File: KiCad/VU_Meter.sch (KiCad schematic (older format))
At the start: 34 parts

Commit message: changed Q to a fixed value
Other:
- moved on the sheet: D?, R?, U?

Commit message: saved from laptop and added new questions
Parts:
- U? (x15): symbol Comparator:LM393 -> Amp-Module-rescue:LM393-Comparator
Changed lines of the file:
@@
 $EndDescr
 $Comp
-L Comparator:LM393 U?
+L Amp-Module-rescue:LM393-Comparator U?
 U 3 1 60442CB7
 P 8200 4050
+AR Path="/60442CB7" Ref="U?"  Part="3"
+AR Path="/603D6377/60442CB7" Ref="U?"  Part="3"
 F 0 "U?" V 7900 4050 50  0000 C CNN
 F 1 "LM393" V 8000 4050 50  0000 C CNN
@@
 +5VDC
 $Comp
-L Comparator:LM393 U?
+L Amp-Module-rescue:LM393-Comparator U?
 U 1 1 60442CBE
 P 10400 3750
+AR Path="/60442CBE" Ref="U?"  Part="1"
+AR Path="/603D6377/60442CBE" Ref="U?"  Part="1"
 F 0 "U?" H 10400 3950 50  0000 C CNN
 F 1 "LM393" H 10400 3750 50  0000 C CNN
@@
 $EndComp
 $Comp
-L Comparator:LM393 U?
+L Amp-Module-rescue:LM393-Comparator U?
 U 2 1 60442CC4
 P 10400 4250
+AR Path="/60442CC4" Ref="U?"  Part="2"
+AR Path="/603D6377/60442CC4" Ref="U?"  Part="2"
 F 0 "U?" H 10400 4450 50  0000 C CNN
 F 1 "LM393" H 10400 4250 50  0000 C CNN
@@
 $EndComp
 $Comp
-L Comparator:LM393 U?
+L Amp-Module-rescue:LM393-Comparator U?
 U 2 1 60442CCA
 P 10400 5250
+AR Path="/60442CCA" Ref="U?"  Part="2"
+AR Path="/603D6377/60442CCA" Ref="U?"  Part="2"
 F 0 "U?" H 10400 5450 50  0000 C CNN
 F 1 "LM393" H 10400 5250 50  0000 C CNN
@@
 VOUT MONITOR
 $Comp
-L Comparator:LM393 U?
+L Amp-Module-rescue:LM393-Comparator U?
 U 3 1 60442D23
 P 8200 4400
+AR Path="/60442D23" Ref="U?"  Part="3"
+AR Path="/603D6377/60442D23" Ref="U?"  Part="3"
 F 0 "U?" V 7900 4400 50  0000 C CNN
 F 1 "LM393" V 8000 4400 50  0000 C CNN
@@
 $EndComp
 $Comp
-L Comparator:LM393 U?
+L Amp-Module-rescue:LM393-Comparator U?
 U 3 1 60442D29
 P 8200 4750
+AR Path="/60442D29" Ref="U?"  Part="3"
+AR Path="/603D6377/60442D29" Ref="U?"  Part="3"
 F 0 "U?" V 7900 4750 50  0000 C CNN
 F 1 "LM393" V 8000 4750 50  0000 C CNN
@@
 $EndComp
 $Comp
-L Comparator:LM393 U?
+L Amp-Module-rescue:LM393-Comparator U?
 U 3 1 60442D2F
 P 8200 5100
+AR Path="/60442D2F" Ref="U?"  Part="3"
+AR Path="/603D6377/60442D2F" Ref="U?"  Part="3"
 F 0 "U?" V 7900 5100 50  0000 C CNN
 F 1 "LM393" V 8000 5100 50  0000 C CNN
@@
 $EndComp
 $Comp
-L Comparator:LM393 U?
+L Amp-Module-rescue:LM393-Comparator U?
 U 3 1 60442D35
 P 8200 5450
+AR Path="/60442D35" Ref="U?"  Part="3"
+AR Path="/603D6377/60442D35" Ref="U?"  Part="3"
 F 0 "U?" V 7900 5450 50  0000 C CNN
 F 1 "LM393" V 8000 5450 50  0000 C CNN
@@
 $EndComp
 $Comp
-L Comparator:LM393 U?
+L Amp-Module-rescue:LM393-Comparator U?
 U 1 1 60442D72
 P 10400 4750
+AR Path="/60442D72" Ref="U?"  Part="1"
+AR Path="/603D6377/60442D72" Ref="U?"  Part="1"
 F 0 "U?" H 10400 4950 50  0000 C CNN
 F 1 "LM393" H 10400 4750 50  0000 C CNN
@@
 	9950 5150 9950 5200
 $Comp
-L Comparator:LM393 U?
+L Amp-Module-rescue:LM393-Comparator U?
 U 1 1 60442D88
 P 10400 1200
+AR Path="/60442D88" Ref="U?"  Part="1"
+AR Path="/603D6377/60442D88" Ref="U?"  Part="1"
 F 0 "U?" H 10400 1400 50  0000 C CNN
 F 1 "LM393" H 10400 1200 50  0000 C CNN
@@
 $EndComp
 $Comp
-L Comparator:LM393 U?
+L Amp-Module-rescue:LM393-Comparator U?
 U 2 1 60442D8E
 P 10400 1700
+AR Path="/60442D8E" Ref="U?"  Part="2"
+AR Path="/603D6377/60442D8E" Ref="U?"  Part="2"
 F 0 "U?" H 10400 1900 50  0000 C CNN
 F 1 "LM393" H 10400 1700 50  0000 C CNN
@@
 $EndComp
 $Comp
-L Comparator:LM393 U?
+L Amp-Module-rescue:LM393-Comparator U?
 U 2 1 60442D94
 P 10400 2700
+AR Path="/60442D94" Ref="U?"  Part="2"
+AR Path="/603D6377/60442D94" Ref="U?"  Part="2"
 F 0 "U?" H 10400 2900 50  0000 C CNN
 F 1 "LM393" H 10400 2700 50  0000 C CNN
@@
 	11050 1200 11050 1700
 $Comp
-L Comparator:LM393 U?
+L Amp-Module-rescue:LM393-Comparator U?
 U 1 1 60442DEA
 P 10400 2200
+AR Path="/60442DEA" Ref="U?"  Part="1"
+AR Path="/603D6377/60442DEA" Ref="U?"  Part="1"
 F 0 "U?" H 10400 2400 50  0000 C CNN
 F 1 "LM393" H 10400 2200 50  0000 C CNN
@@
 LM_VOUT3MON
 $Comp
-L Comparator:LM393 U?
+L Amp-Module-rescue:LM393-Comparator U?
 U 1 1 60442E29
 P 8650 2750
+AR Path="/60442E29" Ref="U?"  Part="1"
+AR Path="/603D6377/60442E29" Ref="U?"  Part="1"
 F 0 "U?" H 8650 2950 50  0000 C CNN
 F 1 "LM393" H 8650 2750 50  0000 C CNN
@@
 $EndComp
 $Comp
-L Comparator:LM393 U?
+L Amp-Module-rescue:LM393-Comparator U?
 U 2 1 60442E2F
 P 8650 3400
+AR Path="/60442E2F" Ref="U?"  Part="2"
+AR Path="/603D6377/60442E2F" Ref="U?"  Part="2"
 F 0 "U?" H 8650 3600 50  0000 C CNN
 F 1 "LM393" H 8650 3400 50  0000 C CNN

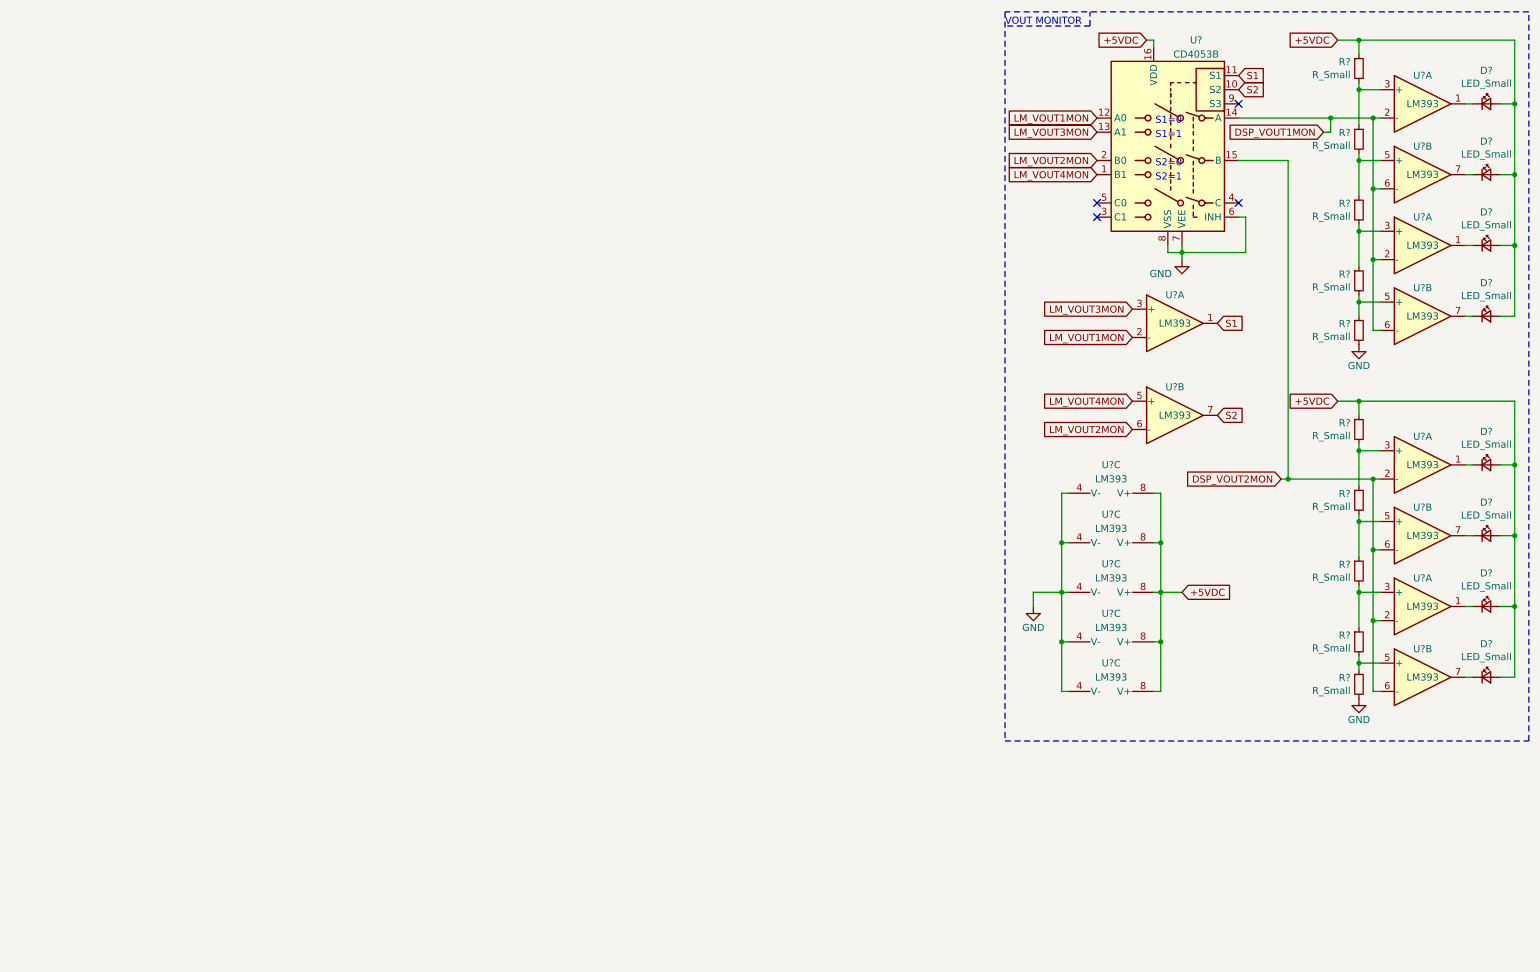
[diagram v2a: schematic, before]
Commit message: removed VU Meter sheet
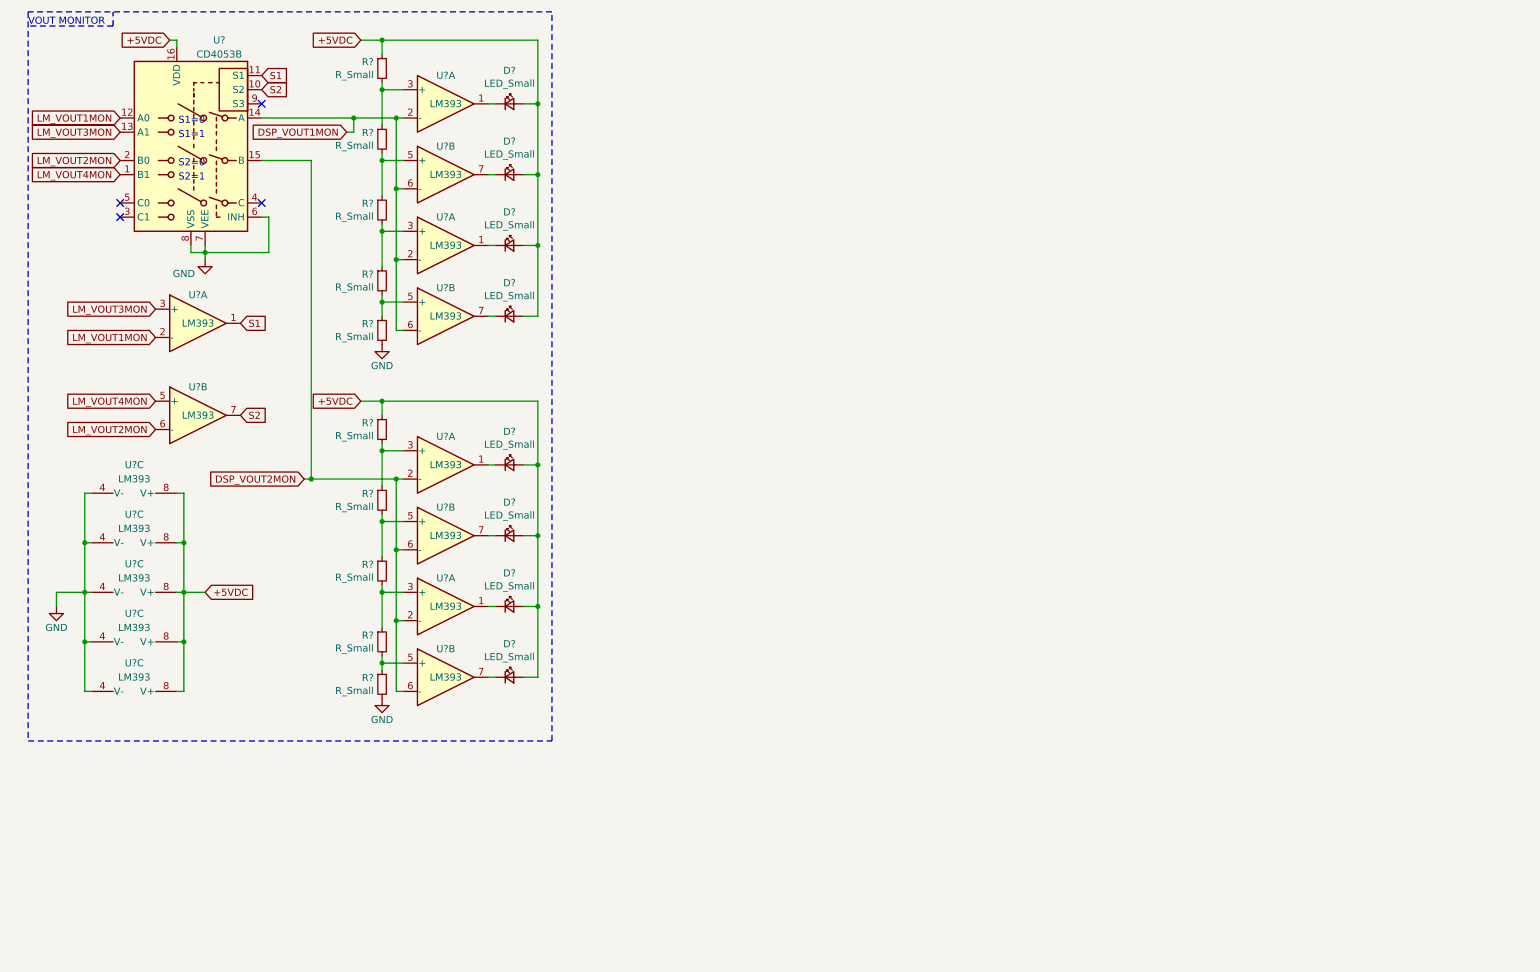
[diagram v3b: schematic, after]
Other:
- moved on the sheet: D?, R?, U?, U?A, U?B, U?C

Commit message: added custom VU meter
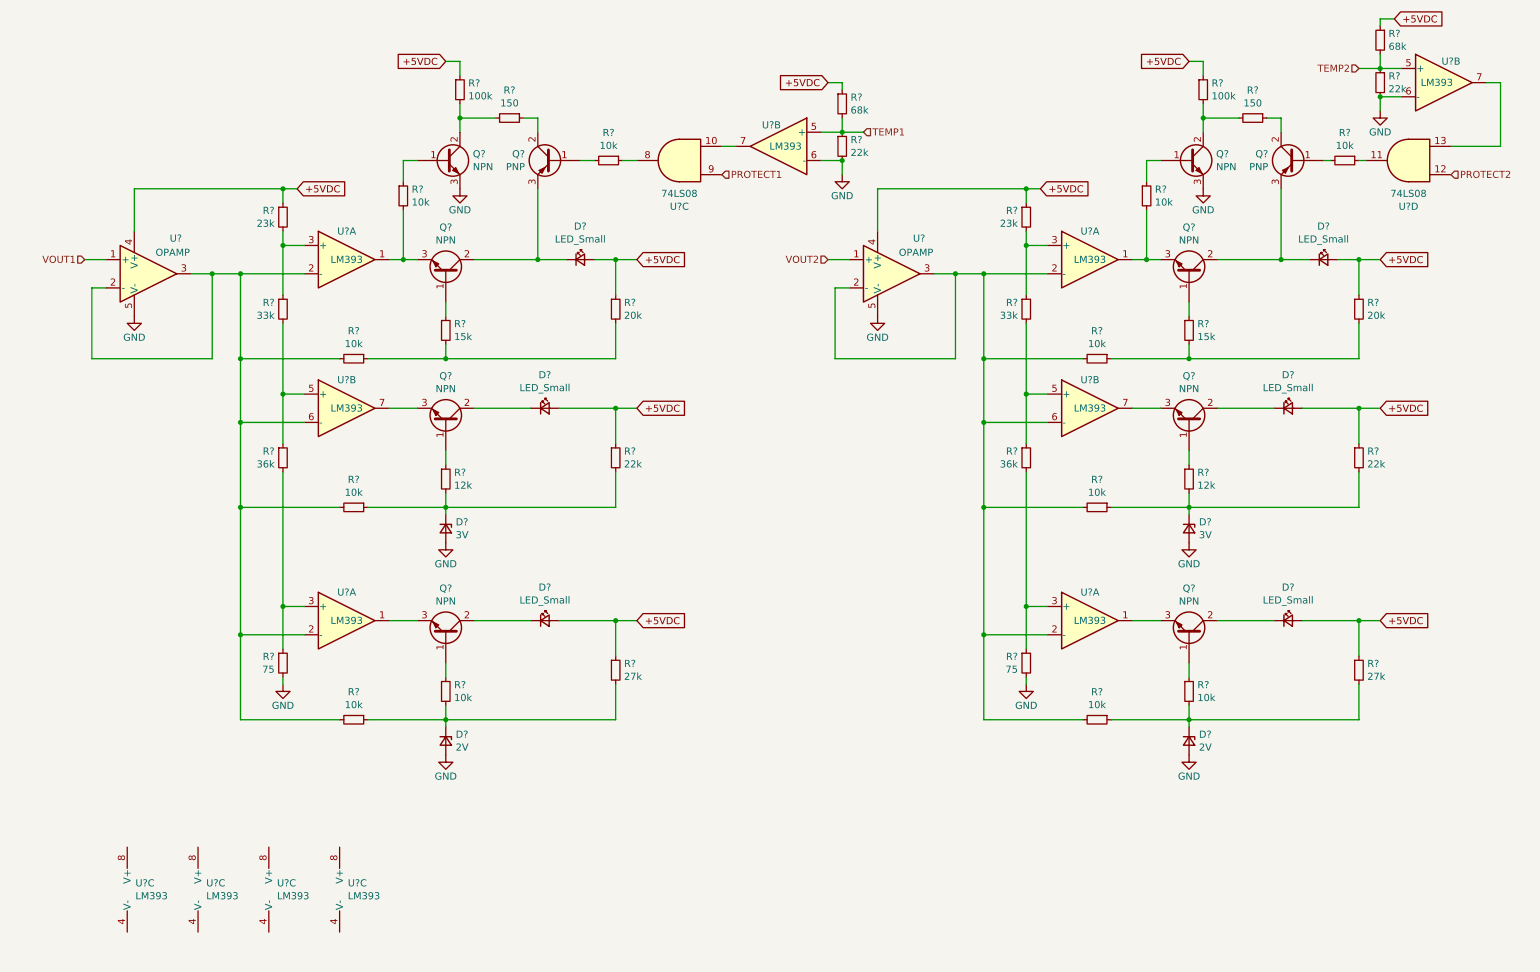
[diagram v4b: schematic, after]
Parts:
- removed D? (x7): LED_Small, symbol Device:LED_Small
- removed R? (x9): R_Small, symbol Device:R_Small
- removed U? (x12): LM393, symbol Amp-Module-rescue:LM393-Comparator
- removed U?: CD4053B, symbol Analog_Switch:CD4053B
- added D? (x5): LED_Small, symbol Device:LED_Small
- added D? (x2): 3V, symbol Device:D_Zener_Small
- added D? (x2): 2V, symbol Device:D_Zener_Small
- added Q? (x8): NPN, symbol Device:Q_NPN_BCE
- added Q? (x2): PNP, symbol Device:Q_PNP_BCE
- added R? (x2): 20k, symbol Device:R_Small
- added R? (x2): 15k, symbol Device:R_Small
- added R? (x2): 23k, symbol Device:R_Small
- added R? (x12): 10k, symbol Device:R_Small
- added R? (x2): 100k, symbol Device:R_Small
- added R? (x2): 150, symbol Device:R_Small
- added R? (x4): 22k, symbol Device:R_Small
- added R? (x2): 12k, symbol Device:R_Small
- added R? (x2): 33k, symbol Device:R_Small
- added R? (x2): 27k, symbol Device:R_Small
- added R? (x2): 36k, symbol Device:R_Small
- added R?: 75, symbol Device:R_Small
- added R? (x2): 68k, symbol Device:R_Small
- added U? (x2): OPAMP, symbol pspice:OPAMP
- added U? (x9): LM393, symbol Amp-Module-rescue:LM393-Comparator
- added U? (x2): 74LS08, symbol 74xx:74LS08
- R?: value R_Small -> 75
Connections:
- net +5VDC: now also D?.2 (A), D?.2 (A), D?.2 (A), D?.2 (A), D?.2 (A), R?.1, R?.1, R?.1, R?.1, R?.1, R?.1, R?.1, R?.1, R?.1, R?.1, R?.1, R?.1, U?.4 (V+), U?.4 (V+)
- net GND: now also R?.2, D?.2 (A), D?.2 (A), D?.2 (A), D?.2 (A), Q?.3 (E), Q?.3 (E), R?.2, R?.2, R?.2, U?.5 (V-), U?.5 (V-), U?.6 (-), U?.6 (-)
- net at U?.1: now also Q?.3 (E), R?.2; no longer D?.1 (K)
- net at U?.3 (+): now also R?.1, R?.2
- net at U?.5 (+): now also R?.1, R?.2
- net at U?.7: now also Q?.3 (E)
- net at R?.1, U?.3 (+): now also R?.2
- net at U?.1: now also Q?.3 (E)
- net DSP_VOUT1MON: no longer names the net of U?.2 (-), U?.2 (-), U?.6 (-)
- net DSP_VOUT1MON: now also R?.2, R?.2, R?.2, U?.2 (-), U?.3
- new net: D?.1 (K), Q?.2 (C), Q?.3 (E) (x2)
- new net: Q?.1 (B), R?.1 (x8)
- new net: R?.1, R?.2, R?.2 (x2)
- new net: Q?.2 (C), R?.2, R?.2 (x2)
- new net: Q?.2 (C), R?.1 (x2)
- new net: Q?.1 (B), R?.2 (x2)
- new net: R?.1, U?.8
- new net: D?.1 (K), Q?.2 (C) (x4)
- new net: D?.1 (K), R?.1, R?.2, R?.2 (x4)
- new net: U?.10, U?.7
- new net: R?.1, U?.11
- new net: U?.13, U?.7
- new net: Q?.3 (E), R?.2, U?.1
- new net: R?.2, R?.2, R?.2, U?.2 (-), U?.2 (-), U?.2 (-), U?.3, U?.6 (-)
- new net: R?.1, R?.2, U?.3 (+) (x2)
- new net: R?.1, R?.2, U?.5 (+)
- new net: Q?.3 (E), U?.7
- new net: Q?.3 (E), U?.1
- new net PROTECT1: U?.9
- new net PROTECT2: U?.12
- new net TEMP1: R?.1, R?.2, U?.5 (+)
- new net TEMP2: R?.1, R?.2, U?.5 (+)
- new net VOUT1: U?.1 (+)
- new net VOUT2: U?.1 (+)
- no-connect marks 4 -> 0
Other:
- note removed: "S1=0"
- note removed: "S1=1"
- note removed: "S2=0"
- note removed: "S2=1"
- note removed: "VOUT MONITOR"
- moved on the sheet: D?, R?, U?A, U?B

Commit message: first single IDC commit
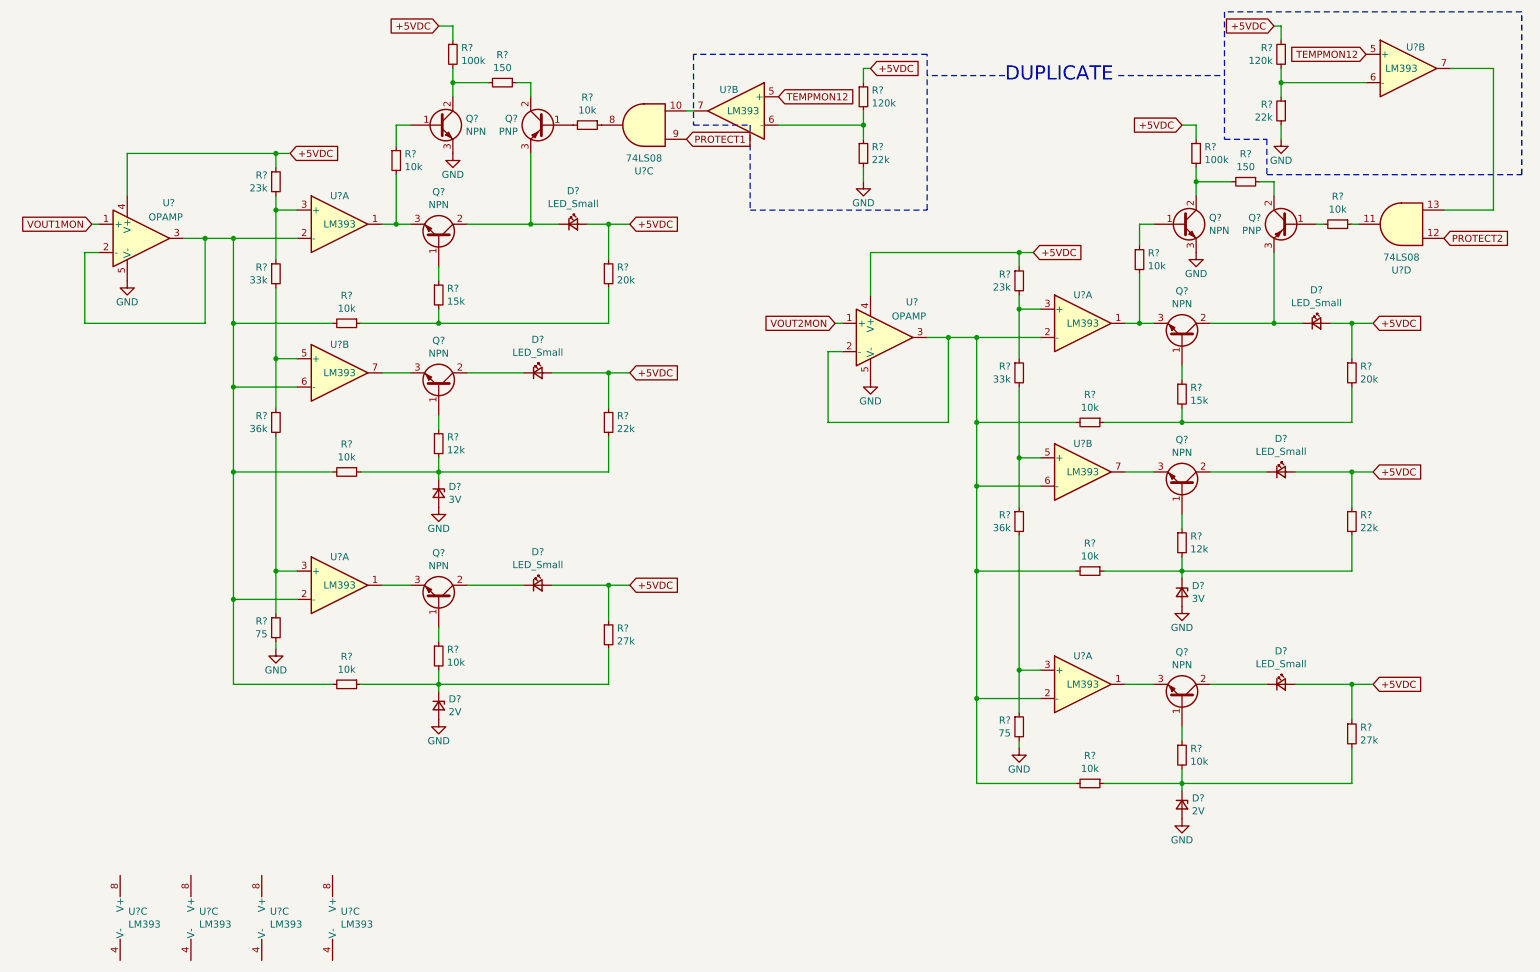
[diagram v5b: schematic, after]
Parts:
- removed D? (x6): LED_Small, symbol Device:LED_Small
- removed D? (x2): 3V, symbol Device:D_Zener_Small
- removed D? (x2): 2V, symbol Device:D_Zener_Small
- removed Q? (x8): NPN, symbol Device:Q_NPN_BCE
- removed Q? (x2): PNP, symbol Device:Q_PNP_BCE
- removed R? (x2): 75, symbol Device:R_Small
- removed R? (x2): 20k, symbol Device:R_Small
- removed R? (x2): 15k, symbol Device:R_Small
- removed R? (x2): 23k, symbol Device:R_Small
- removed R? (x12): 10k, symbol Device:R_Small
- removed R? (x2): 100k, symbol Device:R_Small
- removed R? (x2): 150, symbol Device:R_Small
- removed R? (x4): 22k, symbol Device:R_Small
- removed R? (x2): 12k, symbol Device:R_Small
- removed R? (x2): 33k, symbol Device:R_Small
- removed R? (x2): 27k, symbol Device:R_Small
- removed R? (x2): 36k, symbol Device:R_Small
- removed R? (x2): 68k, symbol Device:R_Small
- removed U? (x12): LM393, symbol Amp-Module-rescue:LM393-Comparator
- removed U? (x2): OPAMP, symbol pspice:OPAMP
- removed U? (x2): 74LS08, symbol 74xx:74LS08
- added D? (x6): LED_Small, symbol Device:LED_Small
- added D? (x2): 3V, symbol Device:D_Zener_Small
- added D? (x2): 2V, symbol Device:D_Zener_Small
- added Q? (x8): NPN, symbol Device:Q_NPN_BCE
- added Q? (x2): PNP, symbol Device:Q_PNP_BCE
- added R? (x2): 75, symbol Device:R_Small
- added R? (x2): 20k, symbol Device:R_Small
- added R? (x2): 15k, symbol Device:R_Small
- added R? (x2): 23k, symbol Device:R_Small
- added R? (x12): 10k, symbol Device:R_Small
- added R? (x2): 100k, symbol Device:R_Small
- added R? (x2): 150, symbol Device:R_Small
- added R? (x4): 22k, symbol Device:R_Small
- added R? (x2): 12k, symbol Device:R_Small
- added R? (x2): 33k, symbol Device:R_Small
- added R? (x2): 27k, symbol Device:R_Small
- added R? (x2): 36k, symbol Device:R_Small
- added R? (x2): 120k, symbol Device:R_Small
- added U? (x12): LM393, symbol Amp-Module-rescue:LM393-Comparator-Amp-Module-rescue
- added U? (x2): OPAMP, symbol pspice:OPAMP
- added U? (x2): 74LS08, symbol 74xx:74LS08
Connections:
- net +5VDC: now also D?.2 (A), D?.2 (A), D?.2 (A), D?.2 (A), D?.2 (A), D?.2 (A), R?.1, R?.1, R?.1, R?.1, R?.1, R?.1, R?.1, R?.1, R?.1, R?.1, R?.1, R?.1, U?.4 (V+), U?.4 (V+)
- net GND: now also D?.2 (A), D?.2 (A), D?.2 (A), D?.2 (A), Q?.3 (E), Q?.3 (E), R?.2, R?.2, R?.2, R?.2, U?.5 (V-), U?.5 (V-)
- net PROTECT1: now also U?.9
- net PROTECT2: now also U?.12
- new net: Q?.3 (E), R?.2, U?.1 (x2)
- new net: R?.2, R?.2, R?.2, U?.2 (-), U?.2 (-), U?.2 (-), U?.3, U?.6 (-) (x2)
- new net: R?.1, R?.2, U?.3 (+) (x4)
- new net: R?.1, R?.2, U?.5 (+) (x2)
- new net: Q?.3 (E), U?.7 (x2)
- new net: D?.1 (K), Q?.2 (C), Q?.3 (E) (x2)
- new net: Q?.3 (E), U?.1 (x2)
- new net: Q?.1 (B), R?.1 (x8)
- new net: R?.1, R?.2, R?.2 (x2)
- new net: Q?.2 (C), R?.2, R?.2 (x2)
- new net: Q?.2 (C), R?.1 (x2)
- new net: Q?.1 (B), R?.2 (x2)
- new net: R?.1, U?.8
- new net: D?.1 (K), Q?.2 (C) (x4)
- new net: D?.1 (K), R?.1, R?.2, R?.2 (x4)
- new net: R?.1, R?.2, U?.6 (-) (x2)
- new net: U?.10, U?.7
- new net: R?.1, U?.11
- new net: U?.13, U?.7
- new net TEMPMON12: U?.5 (+), U?.5 (+)
- new net VOUT1MON: U?.1 (+)
- new net VOUT2MON: U?.1 (+)
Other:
- note added: "DUPLICATE"
